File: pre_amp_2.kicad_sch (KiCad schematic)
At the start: 55 parts, among them J1 IN, J10 SW2_1, J11 SW2_4, J12 VR5_3, J13 VR5_1, J14 OUT, J2 GND2, J3 Vin, J4 GND, J5 VR2_2, J6 VR3_3, J7 VR1_3, J8 VR4_2, J9 SW2_3, SW1 bright, SW2 SW_SP3T, U1 TL072, U2 TC1044S

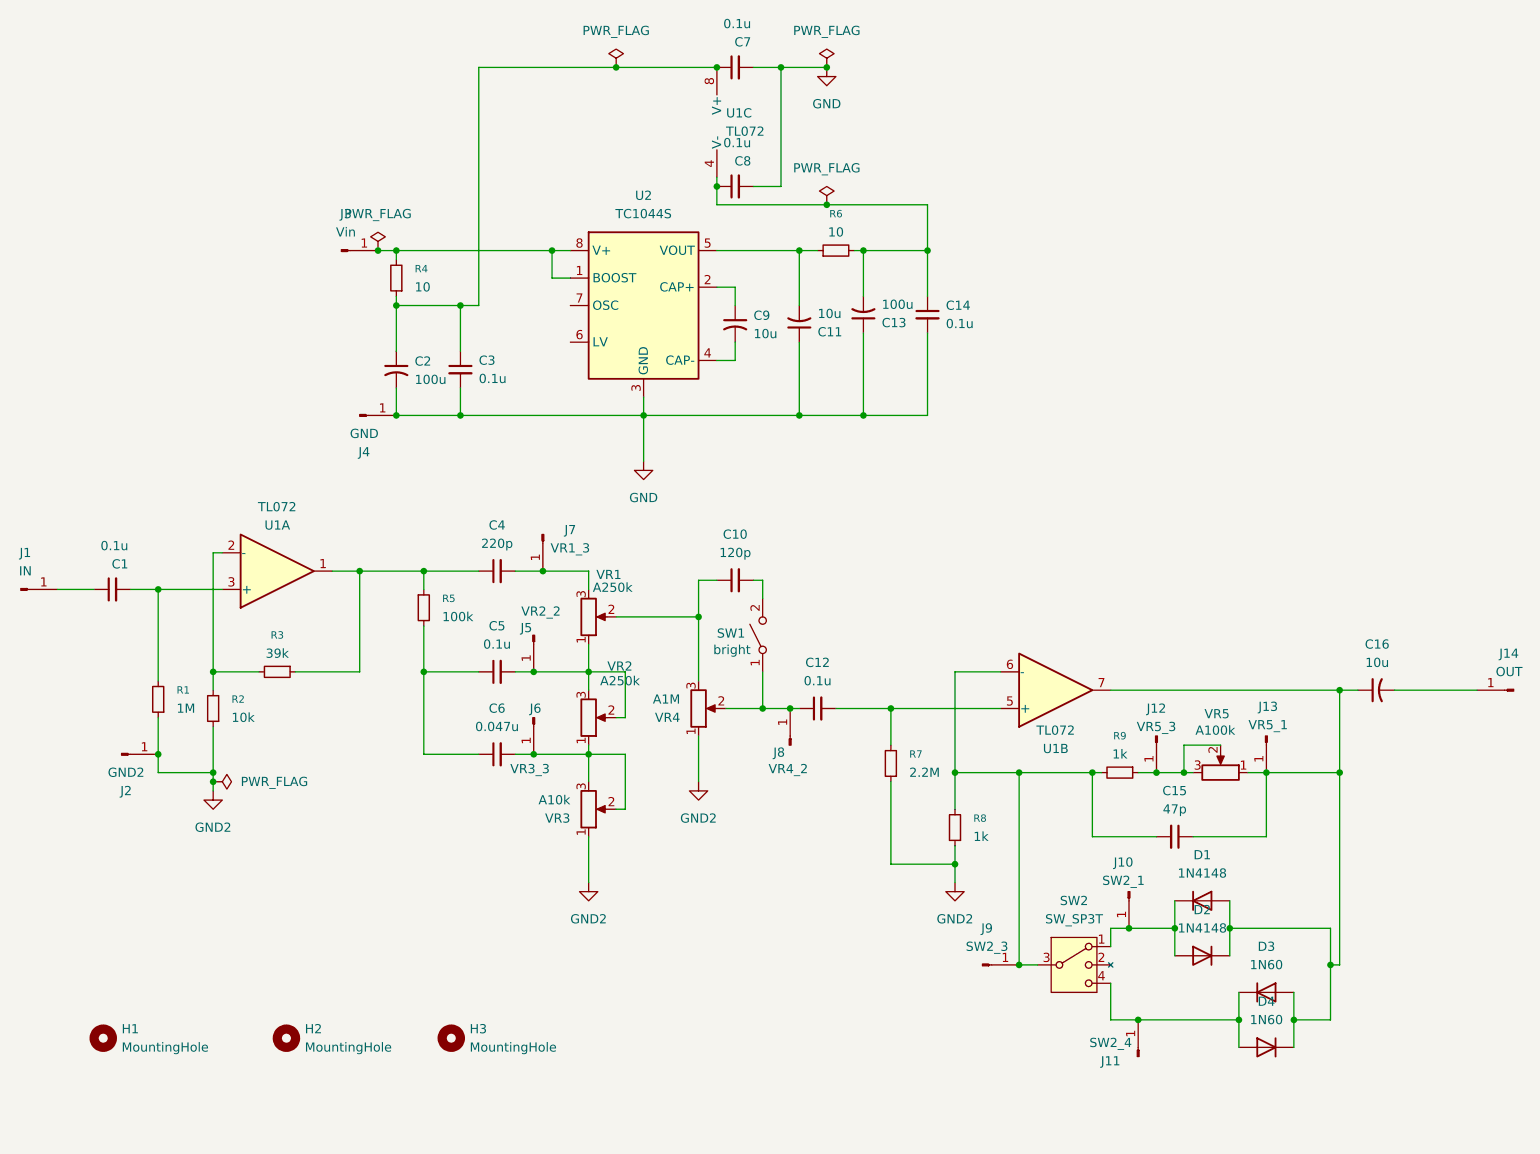
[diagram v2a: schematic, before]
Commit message: R3を47kに変更、シールド線の網線をGNDに繋ぐ配線を追加。
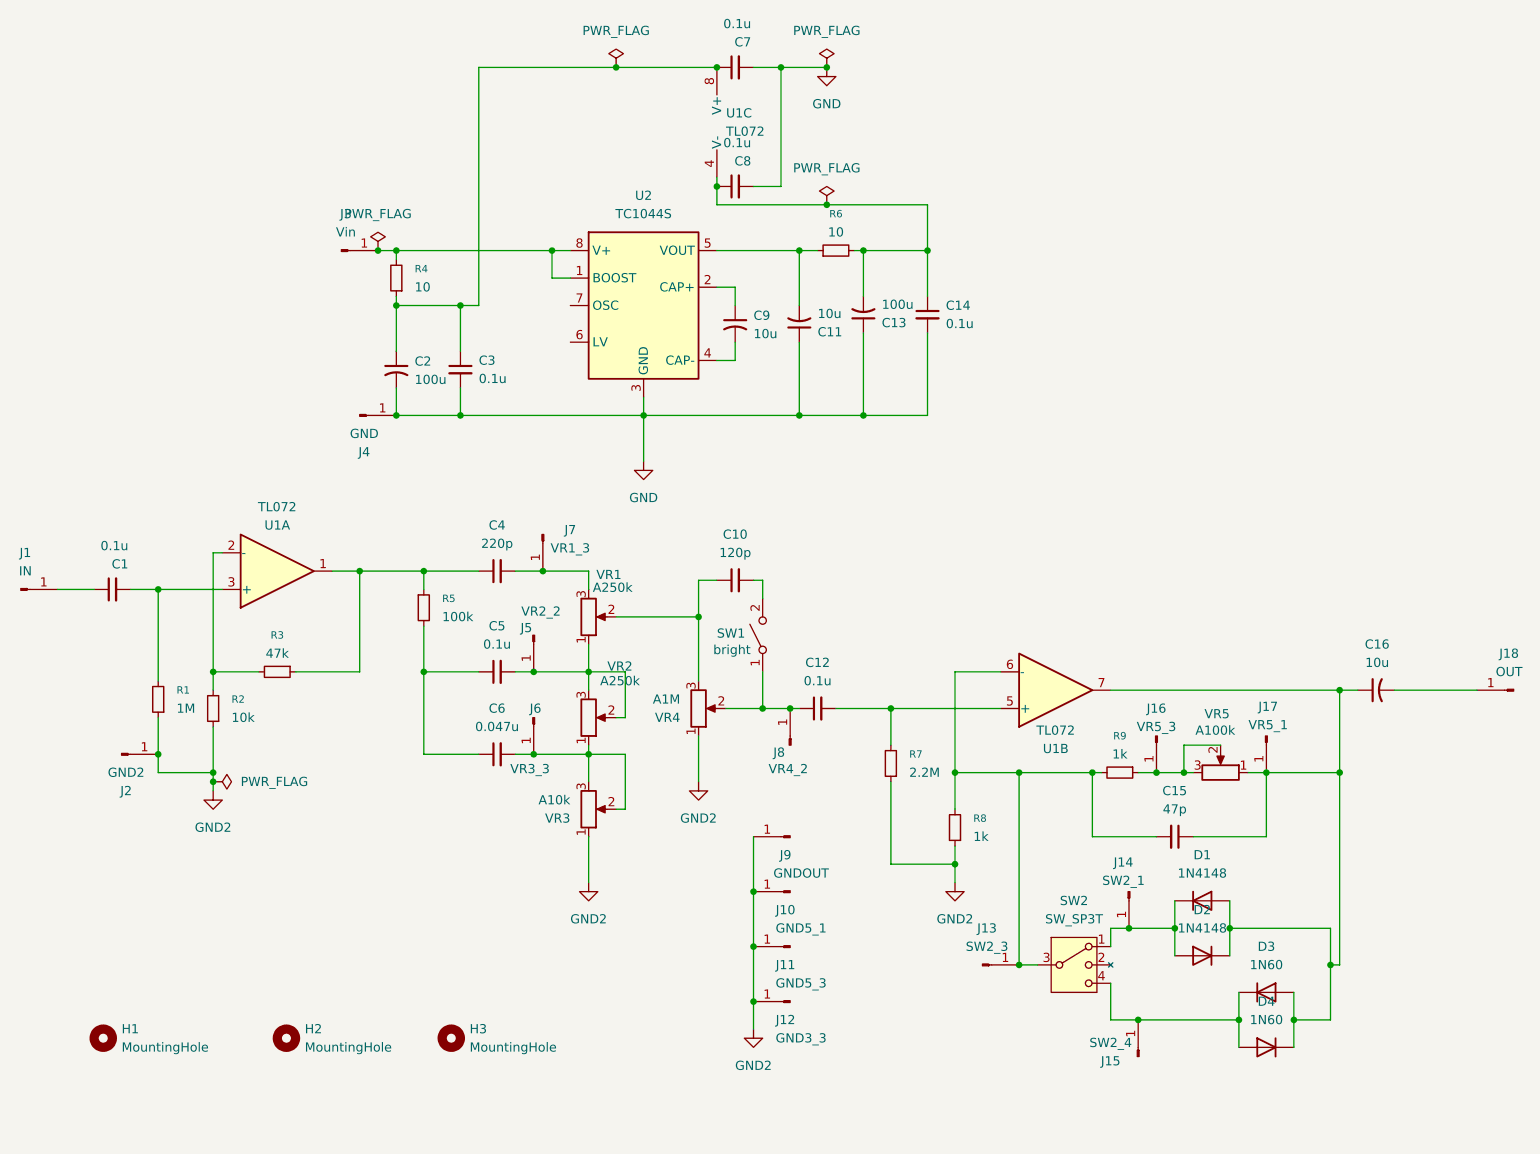
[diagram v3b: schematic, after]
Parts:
- added J10: GND5_1, Connector_PinHeader_2.54mm:PinHeader_1x01_P2.54mm_Vertical, symbol Connector:Conn_01x01_Pin
- added J11: GND5_3, Connector_PinHeader_2.54mm:PinHeader_1x01_P2.54mm_Vertical, symbol Connector:Conn_01x01_Pin
- added J12: GND3_3, Connector_PinHeader_2.54mm:PinHeader_1x01_P2.54mm_Vertical, symbol Connector:Conn_01x01_Pin
- added J9: GNDOUT, Connector_PinHeader_2.54mm:PinHeader_1x01_P2.54mm_Vertical, symbol Connector:Conn_01x01_Pin
- R3: value 39k -> 47k
- renumbered J9 to J13, J10 to J14, J11 to J15, J12 to J16, J13 to J17, J14 to J18
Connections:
- net GND2: now also J10.1 (Pin_1), J11.1 (Pin_1), J12.1 (Pin_1), J9.1 (Pin_1)

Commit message: チャージポンプの抵抗と電解コンデンサを強化
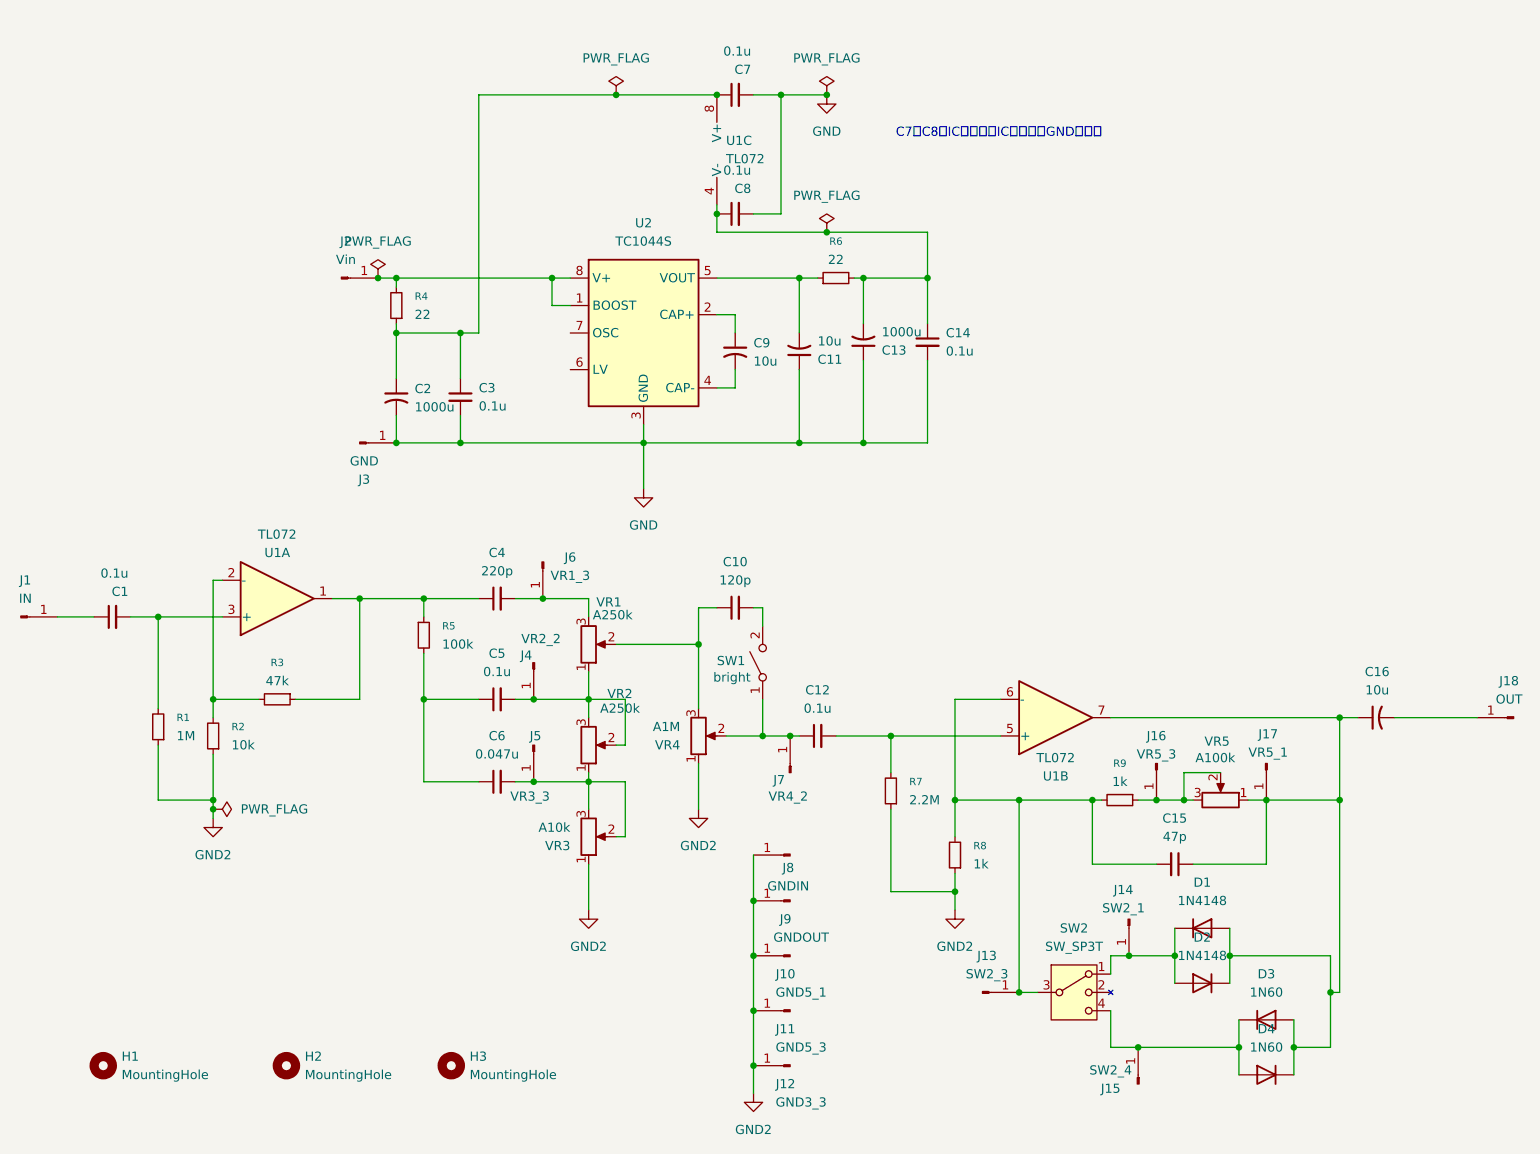
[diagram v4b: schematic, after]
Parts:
- C13, C2: value 100u -> 1000u; footprint Capacitor_THT:CP_Radial_D10.0mm_P2.50mm -> Capacitor_THT:CP_Radial_D10.0mm_P5.00mm
- J8: renamed from J2; value GND2 -> GNDIN
- R4, R6: value 10 -> 22
- renumbered J3 to J2, J4 to J3, J5 to J4, J6 to J5, J7 to J6, J8 to J7
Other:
- note added: "C7、C8はICの裏側でICの足からGNDに直結"
- moved on the sheet: C1, C10, C11, C12, C13, C14, C15, C16, C2, C3, C4, C5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
